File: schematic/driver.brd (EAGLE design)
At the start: 160 x 100 mm, 118 parts, among them IC1 DW01A, IC2 DW01A, IC3 DW01A, IC4 MPU6050, Q2 SI1922EDH-T1-GE3, Q3 SI1922EDH-T1-GE3, Q4 SI1922EDH-T1-GE3

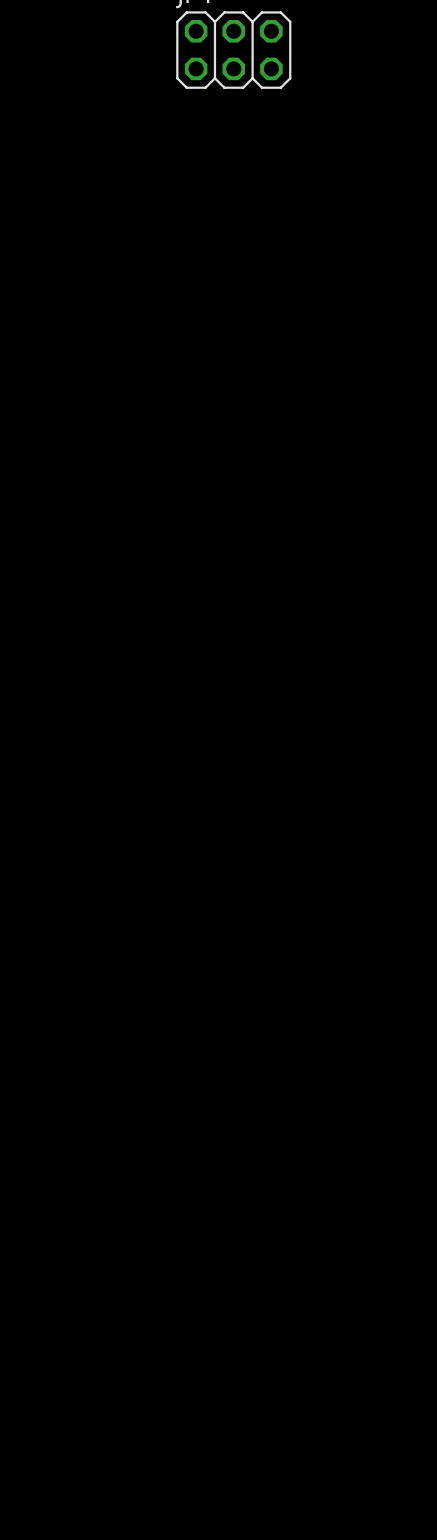
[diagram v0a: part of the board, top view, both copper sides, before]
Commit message: Added piheads for sensors. Added transoptors.
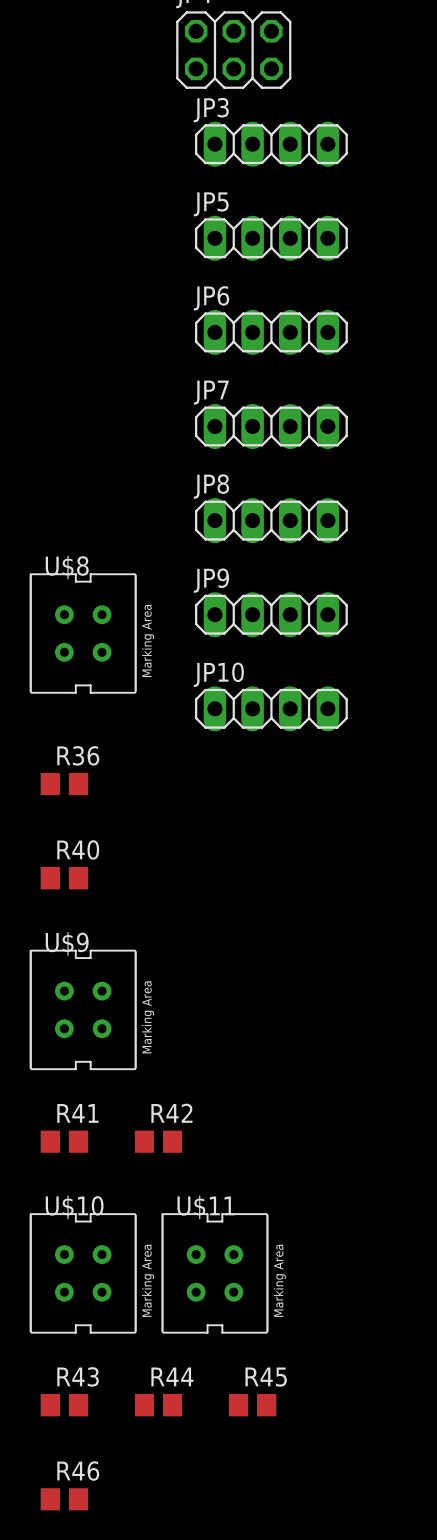
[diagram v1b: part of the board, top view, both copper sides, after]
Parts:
- added JP10, JP3, JP5, JP6, JP7, JP8, JP9: (no value), pinhead:1X04
- added R36, R41, R43, R45: 20k, rcl:R0805
- added R40, R42, R44, R46: 200, rcl:R0805
- added U$10, U$11, U$8, U$9: CNY70, cny70:4
- R35: value 50 -> 50k
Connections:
- removed net LED2: STM32.12
- removed net N$17: STM32.29
- removed net PB9: 3.3V1.A, S2.3
- removed net PC13: STM32.2
- removed net PC14: 3.3V2.A, S2.2, STM32.3
- removed net S0: STM32.18
- removed net TRST: STM32.40
- new net ADC1: R36.1, STM32.11, U$8.C
- new net ADC2: R41.1, STM32.12, U$9.C
- new net ADC3: R43.1, STM32.13, U$10.C
- new net ADC4: R45.1, U$11.C
- new net N$1: R40.1, U$8.A
- new net N$56: R42.1, U$9.A
- new net N$57: STM32.41
- new net N$62: R44.1, U$10.A
- new net N$65: R43.2, R44.2
- new net N$66: R46.1, U$11.A
- new net N$68: R45.2, R46.2
- new net SW1: 3.3V3.A, S2.1, STM32.29
- new net SW2: 3.3V2.A, S2.2, STM32.30
- new net SW3: 3.3V1.A, S2.3, STM32.31
- net BAT: now also STM32.10; no longer STM32.13
- net BUT: now also STM32.18, STM32.3; no longer STM32.19
- net GND: now also JP10.2, JP3.2, JP5.2, JP6.2, JP7.2, JP8.2, JP9.2, U$10.E, U$10.K, U$11.E, U$11.K, U$8.E, U$8.K, U$9.E, U$9.K
- net INT: now also STM32.19; no longer STM32.39
- net LED1: now also STM32.2, STM32.39, STM32.40; no longer STM32.11
- net PC15: no longer 3.3V3.A, S2.1
- net SCL2: now also JP10.3, JP3.3, JP5.3, JP6.3, JP7.3, JP8.3, JP9.3
- net SDA2: now also JP10.4, JP3.4, JP5.4, JP6.4, JP7.4, JP8.4, JP9.4
- net VCC: now also JP10.1, JP3.1, JP5.1, JP6.1, JP7.1, JP8.1, JP9.1, R36.2, R40.2, R41.2, R42.2

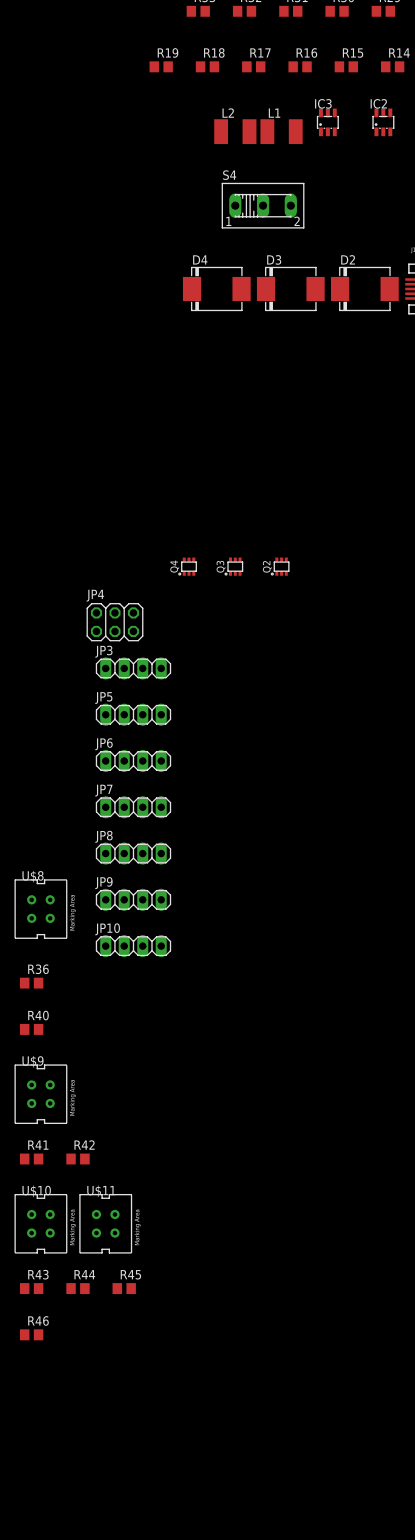
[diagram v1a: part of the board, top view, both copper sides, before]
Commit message: Pull up resistors to two I2C buses
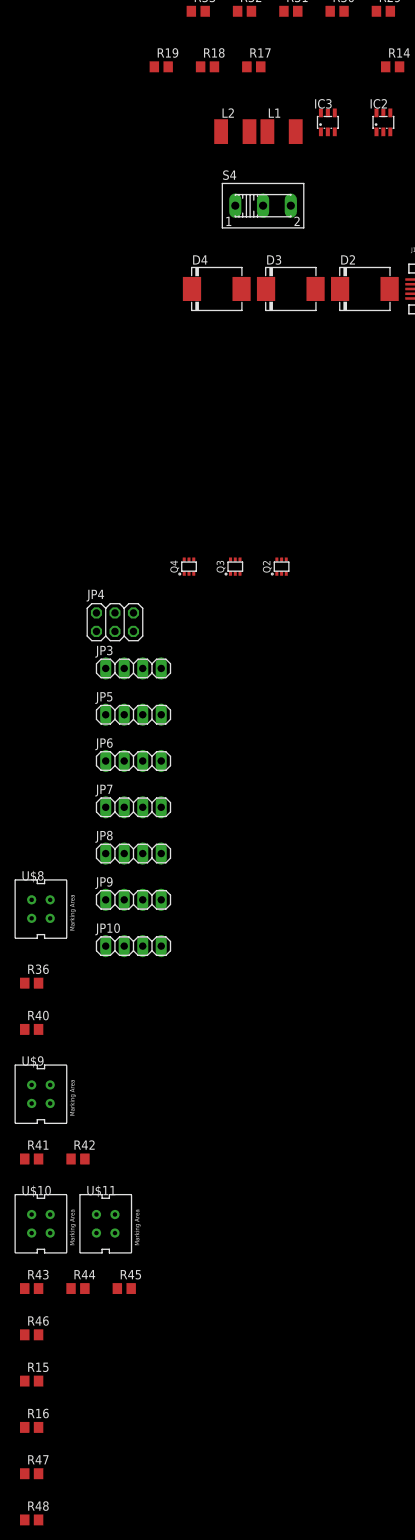
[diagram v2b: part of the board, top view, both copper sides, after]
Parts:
- added R47: 4.7k, rcl:R0805
- added R48: 4.7, rcl:R0805
- R15: value 4k7 -> 4.7k
- R16: value 4k7 -> 4.7
- moved R16 190.3 mm to (-121.9, -110.5)
- moved R15 185.4 mm to (-121.9, -104.1)
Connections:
- net SCL: no longer IC4.23, R16.1
- net SCL1: now also IC4.23, R47.1
- net SCL2: now also R15.1
- net SDA: no longer IC4.24, R15.1
- net SDA1: now also IC4.24, R48.1
- net SDA2: now also R16.1
- net VCC: no longer R15.2, R16.2
- net VDD: now also R15.2, R16.2, R47.2, R48.2
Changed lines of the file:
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@@
 <attribute name="VALUE" x="-73.025" y="73.66" size="1.27" layer="27"/>
-</element>
-<element name="R15" library="rcl" library_urn="urn:adsk.eagle:library:334" package="R0805" package3d_urn="urn:adsk.eagle:package:23553/2" value="4k7" x="-78.74" y="76.2" smashed="yes">
-<attribute name="NAME" x="-79.375" y="77.47" size="1.27" layer="25"/>
-<attribute name="POPULARITY" value="86" x="0" y="0" size="1.778" layer="27" display="off"/>
-<attribute name="SPICEPREFIX" value="R" x="0" y="0" size="1.778" layer="27" display="off"/>
-<attribute name="VALUE" x="-79.375" y="73.66" size="1.27" layer="27"/>
-</element>
-<element name="R16" library="rcl" library_urn="urn:adsk.eagle:library:334" package="R0805" package3d_urn="urn:adsk.eagle:package:23553/2" value="4k7" x="-85.09" y="76.2" smashed="yes">
-<attribute name="NAME" x="-85.725" y="77.47" size="1.27" layer="25"/>
-<attribute name="POPULARITY" value="86" x="0" y="0" size="1.778" layer="27" display="off"/>
-<attribute name="SPICEPREFIX" value="R" x="0" y="0" size="1.778" layer="27" display="off"/>
-<attribute name="VALUE" x="-85.725" y="73.66" size="1.27" layer="27"/>
 </element>
 <element name="R17" library="rcl" library_urn="urn:adsk.eagle:library:334" package="R0805" package3d_urn="urn:adsk.eagle:package:23553/2" value="10k" x="-91.44" y="76.2" smashed="yes">
@@
 <attribute name="SPICEPREFIX" value="R" x="-139.7" y="-99.06" size="1.778" layer="27" display="off"/>
 <attribute name="VALUE" x="-122.555" y="-100.33" size="1.27" layer="27"/>
+</element>
+<element name="R15" library="rcl" library_urn="urn:adsk.eagle:library:334" package="R0805" package3d_urn="urn:adsk.eagle:package:23553/2" value="4.7k" x="-121.92" y="-104.14" smashed="yes">
+<attribute name="NAME" x="-122.555" y="-102.87" size="1.27" layer="25"/>
+<attribute name="POPULARITY" value="86" x="-121.92" y="-104.14" size="1.778" layer="27" display="off"/>
+<attribute name="SPICEPREFIX" value="R" x="-121.92" y="-104.14" size="1.778" layer="27" display="off"/>
+<attribute name="VALUE" x="-122.555" y="-106.68" size="1.27" layer="27"/>
+</element>
+<element name="R16" library="rcl" library_urn="urn:adsk.eagle:library:334" package="R0805" package3d_urn="urn:adsk.eagle:package:23553/2" value="4.7" x="-121.92" y="-110.49" smashed="yes">
+<attribute name="NAME" x="-122.555" y="-109.22" size="1.27" layer="25"/>
+<attribute name="POPULARITY" value="86" x="-121.92" y="-110.49" size="1.778" layer="27" display="off"/>
+<attribute name="SPICEPREFIX" value="R" x="-121.92" y="-110.49" size="1.778" layer="27" display="off"/>
+<attribute name="VALUE" x="-122.555" y="-113.03" size="1.27" layer="27"/>
+</element>
+<element name="R47" library="rcl" library_urn="urn:adsk.eagle:library:334" package="R0805" package3d_urn="urn:adsk.eagle:package:23553/2" value="4.7k" x="-121.92" y="-116.84" smashed="yes">
+<attribute name="NAME" x="-122.555" y="-115.57" size="1.27" layer="25"/>
+<attribute name="POPULARITY" value="86" x="-121.92" y="-116.84" size="1.778" layer="27" display="off"/>
+<attribute name="SPICEPREFIX" value="R" x="-121.92" y="-116.84" size="1.778" layer="27" display="off"/>
+<attribute name="VALUE" x="-122.555" y="-119.38" size="1.27" layer="27"/>
+</element>
+<element name="R48" library="rcl" library_urn="urn:adsk.eagle:library:334" package="R0805" package3d_urn="urn:adsk.eagle:package:23553/2" value="4.7" x="-121.92" y="-123.19" smashed="yes">
+<attribute name="NAME" x="-122.555" y="-121.92" size="1.27" layer="25"/>
+<attribute name="POPULARITY" value="86" x="-121.92" y="-123.19" size="1.778" layer="27" display="off"/>
+<attribute name="SPICEPREFIX" value="R" x="-121.92" y="-123.19" size="1.778" layer="27" display="off"/>
+<attribute name="VALUE" x="-122.555" y="-125.73" size="1.27" layer="27"/>
 </element>
 </elements>
@@
 <contactref element="C4" pad="1"/>
 <contactref element="C5" pad="1"/>
-<wire x1="-113.03" y1="-1.27" x2="-113.03" y2="1.27" width="0" layer="19" extent="1-1"/>
+<contactref element="R15" pad="2"/>
+<contactref element="R16" pad="2"/>
+<contactref element="R47" pad="2"/>
+<contactref element="R48" pad="2"/>
+<wire x1="-120.97" y1="-116.84" x2="-120.97" y2="-123.19" width="0" layer="19" extent="1-1"/>
+<wire x1="-120.97" y1="-110.49" x2="-120.97" y2="-116.84" width="0" layer="19" extent="1-1"/>
+<wire x1="-120.97" y1="-104.14" x2="-120.97" y2="-110.49" width="0" layer="19" extent="1-1"/>
+<wire x1="-113.03" y1="-1.27" x2="-120.97" y2="-104.14" width="0" layer="19" extent="1-1"/>
+<wire x1="-113.03" y1="1.27" x2="-113.03" y2="-1.27" width="0" layer="19" extent="1-1"/>
 <wire x1="-61.67" y1="47.97" x2="-113.03" y2="1.27" width="0" layer="19" extent="1-1"/>
 <wire x1="-55.17" y1="47.97" x2="-61.67" y2="47.97" width="0" layer="19" extent="1-1"/>
@@
 <signal name="SCL">
 <contactref element="I2C_CON" pad="2"/>
-<contactref element="R16" pad="1"/>
-<contactref element="IC4" pad="23"/>
-<wire x1="-44.45" y1="95.25" x2="-32.45" y2="95.77" width="0" layer="19" extent="1-1"/>
-<wire x1="-86.04" y1="76.2" x2="-44.45" y2="95.25" width="0" layer="19" extent="1-1"/>
 </signal>
 <signal name="SDA">
 <contactref element="I2C_CON" pad="1"/>
-<contactref element="R15" pad="1"/>
-<contactref element="IC4" pad="24"/>
-<wire x1="-46.99" y1="95.25" x2="-32.45" y2="95.27" width="0" layer="19" extent="1-1"/>
-<wire x1="-79.69" y1="76.2" x2="-46.99" y2="95.25" width="0" layer="19" extent="1-1"/>
 </signal>
 <signal name="LED1">
@@
 </signal>
 <signal name="VCC">
-<contactref element="R16" pad="2"/>
-<contactref element="R15" pad="2"/>
 <contactref element="S2" pad="5"/>
 <contactref element="LCD1" pad="6"/>
@@
 <wire x1="-111.76" y1="-12.7" x2="-111.76" y2="-19.05" width="0" layer="19" extent="1-1"/>
 <wire x1="-111.76" y1="-6.35" x2="-111.76" y2="-12.7" width="0" layer="19" extent="1-1"/>
-<wire x1="-84.14" y1="76.2" x2="-111.76" y2="-6.35" width="0" layer="19" extent="1-1"/>
-<wire x1="-77.79" y1="76.2" x2="-84.14" y2="76.2" width="0" layer="19" extent="1-1"/>
-<wire x1="-67.31" y1="95.25" x2="-77.79" y2="76.2" width="0" layer="19" extent="1-1"/>
+<wire x1="-34.02" y1="36.05" x2="-111.76" y2="-6.35" width="0" layer="19" extent="1-1"/>
+<wire x1="-33.02" y1="49.53" x2="-34.02" y2="36.05" width="0" layer="19" extent="1-1"/>
+<wire x1="-23.27" y1="76.2" x2="-33.02" y2="49.53" width="0" layer="19" extent="1-1"/>
+<wire x1="-46.04" y1="76.2" x2="-23.27" y2="76.2" width="0" layer="19" extent="1-1"/>
+<wire x1="-52.39" y1="90.17" x2="-46.04" y2="76.2" width="0" layer="19" extent="1-1"/>
+<wire x1="-67.31" y1="95.25" x2="-52.39" y2="90.17" width="0" layer="19" extent="1-1"/>
 <wire x1="-69.43" y1="107.95" x2="-67.31" y2="95.25" width="0" layer="19" extent="1-1"/>
 <wire x1="-75.78" y1="107.95" x2="-69.43" y2="107.95" width="0" layer="19" extent="1-1"/>
 <wire x1="-82.13" y1="102.87" x2="-75.78" y2="107.95" width="0" layer="19" extent="1-1"/>
-<wire x1="-52.39" y1="90.17" x2="-67.31" y2="95.25" width="0" layer="19" extent="1-1"/>
-<wire x1="-46.04" y1="76.2" x2="-52.39" y2="90.17" width="0" layer="19" extent="1-1"/>
-<wire x1="-23.27" y1="76.2" x2="-46.04" y2="76.2" width="0" layer="19" extent="1-1"/>
-<wire x1="-33.02" y1="49.53" x2="-23.27" y2="76.2" width="0" layer="19" extent="1-1"/>
-<wire x1="-34.02" y1="36.05" x2="-33.02" y2="49.53" width="0" layer="19" extent="1-1"/>
 <wire x1="48.17" y1="72.0875" x2="-23.27" y2="76.2" width="0" layer="19" extent="1-16"/>
 <wire x1="48.17" y1="71.4375" x2="48.17" y2="72.0875" width="0" layer="19" extent="16-16"/>
@@
 <signal name="SCL1">
 <contactref element="STM32" pad="42"/>
+<contactref element="IC4" pad="23"/>
+<contactref element="R47" pad="1"/>
+<wire x1="-32.45" y1="95.77" x2="-122.87" y2="-116.84" width="0" layer="19" extent="1-1"/>
+<wire x1="37.648759375" y1="50.33479375" x2="-32.45" y2="95.77" width="0" layer="19" extent="1-16"/>
 </signal>
 <signal name="SDA1">
 <contactref element="STM32" pad="43"/>
+<contactref element="IC4" pad="24"/>
+<contactref element="R48" pad="1"/>
+<wire x1="37.29520625" y1="49.981240625" x2="-122.87" y2="-123.19" width="0" layer="19" extent="1-16"/>
+<wire x1="-32.45" y1="95.27" x2="37.29520625" y2="49.981240625" width="0" layer="19" extent="1-16"/>
 </signal>
 <signal name="BOOT0">
@@
 <contactref element="JP6" pad="4"/>
 <contactref element="JP5" pad="4"/>
+<contactref element="R16" pad="1"/>
+<wire x1="-104.14" y1="-44.45" x2="-122.87" y2="-110.49" width="0" layer="19" extent="1-1"/>
 <wire x1="-104.14" y1="-38.1" x2="-104.14" y2="-44.45" width="0" layer="19" extent="1-1"/>
 <wire x1="-104.14" y1="-31.75" x2="-104.14" y2="-38.1" width="0" layer="19" extent="1-1"/>
@@
 <contactref element="JP6" pad="3"/>
 <contactref element="JP5" pad="3"/>
+<contactref element="R15" pad="1"/>
+<wire x1="-106.68" y1="-44.45" x2="-122.87" y2="-104.14" width="0" layer="19" extent="1-1"/>
 <wire x1="-106.68" y1="-38.1" x2="-106.68" y2="-44.45" width="0" layer="19" extent="1-1"/>
 <wire x1="-106.68" y1="-31.75" x2="-106.68" y2="-38.1" width="0" layer="19" extent="1-1"/>

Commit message: ułożenie pinów i podpięcie sterowników rage quit
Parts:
- removed 3.3V1, 3.3V2, 3.3V3: (no value), led:CHIPLED_0805
- removed C1, C15, C2, C4, C5: 100n, rcl:C0603
- removed C10, C11: (no value), rcl:C0603
- removed C16: 4,7u, rcl:C0603
- removed I2C_CON, JP10, JP3, JP5, JP6, JP7, JP8, JP9: (no value), pinhead:1X04
- removed Q1: (no value), crystal-geyer_V1_0:3.2X2.5_KX-7
- removed R5, R6, R9: 1k, rcl:R0805
- added BATTERY: (no value), pinhead:1X02
- added CELLS: (no value), Connectors:HDR-04/RA
- added DIS1, DIS2, DIS3, DIS4, DIS5, DIS6, DIS7, JP13, JP14: (no value), pinhead:1X04
- added JP11, JP12: (no value), pinhead:1X03
- added XTAL: (no value), crystal-geyer_V1_0:3.2X2.5_KX-7
- added _C1, _C2: (no value), rcl:C0603
- added _C3, _C4, _C5, _C7: 100n, rcl:C0603
- added _C6: 4,7u, rcl:C0603
- added _C8: 10n, rcl:C0603
- added _C9: 1uF, rcl:C0603
- D2, D3, D4, D5, D6, D7: value S3A -> (none); device s3x_10:DO214AB -> adafruit:CHIPLED-0603-TTW
- JP2: device pinhead:1X02 -> pinhead:2X14
- Q2: value SI1922EDH-T1-GE3 -> MOSFET1
- Q3: value SI1922EDH-T1-GE3 -> MOSFET2
- Q4: value SI1922EDH-T1-GE3 -> MOSFET3
- STM32: value STM32F10XCXT6 -> (none)
- moved U$10 238.2 mm to (86.0, 36.0), flipped to the bottom
- moved L2 230.7 mm to (105.5, -48.5), turned to 90 degrees
- moved L1 219.1 mm to (104.7, -37.7), turned to 90 degrees
- moved R48 215.3 mm to (-105.4, 91.4)
- moved IC3 205.0 mm to (90.0, -44.0)
- moved Q4 201.1 mm to (94.0, -44.0)
- moved R47 201.0 mm to (-66.0, 76.2)
- moved IC1 196.6 mm to (90.0, -51.0)
- moved IC2 194.8 mm to (90.0, -37.0)
- moved JP4 193.8 mm to (81.7, 24.9), turned to 90 degrees
- moved Q3 193.2 mm to (94.0, -37.0)
- moved U$5 191.1 mm to (99.0, -39.0), turned to 90 degrees
- moved Q2 190.9 mm to (94.0, -51.0)
- moved R15 190.8 mm to (-59.7, 76.2)
- moved R46 190.6 mm to (-99.1, 91.4)
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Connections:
- removed net AO1: MB.1, U$7.5, U$7.6, U$7.7, U$7.8
- removed net N$48: C27.1, C28.1, U$6.24
- removed net N$52: 3.3V2.C, R6.2
- removed net N$53: 3.3V3.C, R5.2
- removed net N$57: STM32.41
- removed net SCL: I2C_CON.2
- removed net SDA: I2C_CON.1
- removed net VSS: STM32.8
- new net ...: STM32.25
- new net ADC5: JP11.3, STM32.39
- new net ADC6: JP12.3, STM32.40
- new net N$17: JP14.3
- new net N$64: MB.2, U$7.5, U$7.6, U$7.7, U$7.8
- net A01: now also MA.1; no longer MA.2
- net A02: now also MB.1; no longer MB.2
- net ADC4: now also STM32.19
- net AO2: now also MA.2; no longer MA.1
- net BAT+: now also BATTERY.2; no longer JP2.2
- net BAT_ON: now also C27.1, C28.1, U$6.24
- net BUT: no longer STM32.18
- net CELL1: now also CELLS.2
- net CELL2: now also CELLS.3
- net CELL3: now also CELLS.4
- net GND: now also BATTERY.1, CELLS.1, DIS1.2, DIS2.2, DIS3.2, DIS4.2, DIS5.2, DIS6.2, DIS7.2, JP11.2, JP12.2, JP13.3, S2.1, S2.2, S2.3, STM32.8, _C1.2, _C2.2, _C3.2, _C4.2, _C5.2, _C6.2, _C7.2, _C8.2, _C9.2; no longer C1.2, C10.2, C11.2, C15.2, C16.2, C2.2, C4.2, C5.2, I2C_CON.3, JP10.2, JP2.1, JP3.2, JP5.2, JP6.2, JP7.2, JP8.2, JP9.2, R5.1, R6.1, R9.1
- net INT: now also STM32.18; no longer STM32.19
- net LED1: no longer STM32.39, STM32.40
- net MA1: now also STM32.41; no longer STM32.25
- net MA2: now also STM32.45; no longer STM32.46
- net N$12: now also D2.C@1; no longer D2.C
- net N$14: now also D3.C@1; no longer D3.C
- net N$18: now also D4.C@1; no longer D4.C
- net N$19: now also D5.C@1; no longer D5.C
- net N$2: now also JP14.4; no longer 3.3V1.C, R9.2
- net N$24: now also D6.C@1; no longer D6.C
- net N$25: now also D7.C@1; no longer D7.C
- net N$3: now also XTAL.1, _C2.1; no longer C11.1, Q1.1
- net N$4: now also XTAL.3, _C1.1; no longer C10.1, Q1.3
- net PWMA: now also STM32.46; no longer STM32.45
- net SCL2: now also DIS1.3, DIS2.3, DIS3.3, DIS4.3, DIS5.3, DIS6.3, DIS7.3, JP13.2; no longer JP10.3, JP3.3, JP5.3, JP6.3, JP7.3, JP8.3, JP9.3
- net SDA2: now also DIS1.4, DIS2.4, DIS3.4, DIS4.4, DIS5.4, DIS6.4, DIS7.4, JP13.1; no longer JP10.4, JP3.4, JP5.4, JP6.4, JP7.4, JP8.4, JP9.4
- net SW1: no longer 3.3V3.A, S2.1
- net SW2: no longer 3.3V2.A, S2.2
- net SW3: no longer 3.3V1.A, S2.3
- net SWDA: now also STM32.34
- net SWDIO: no longer STM32.34
- net VCC: now also DIS1.1, DIS2.1, DIS3.1, DIS4.1, DIS5.1, DIS6.1, DIS7.1, JP11.1, JP12.1, JP13.4; no longer JP10.1, JP3.1, JP5.1, JP6.1, JP7.1, JP8.1, JP9.1
- net VCC_S: no longer I2C_CON.4
- net VDD: now also _C3.1, _C4.1, _C5.1, _C6.1, _C7.1, _C8.1, _C9.1; no longer C1.1, C15.1, C16.1, C2.1, C4.1, C5.1
- net VUSB: now also D2.A@1, D3.A@1, D4.A@1, D5.A@1, D6.A@1, D7.A@1; no longer D2.A, D3.A, D4.A, D5.A, D6.A, D7.A
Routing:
- net GND: track 0.00 -> 98.7 mm, vias 0 -> 2
- net BOOT0: track 0.00 -> 39.8 mm
- net PWMA: track 0.00 -> 31.6 mm, vias 0 -> 2
- net VDD: track 0.00 -> 24.6 mm
- net MA2: track 0.00 -> 22.0 mm
- net MA1: track 0.00 -> 20.1 mm, vias 0 -> 2
- net BAT_ON: track 0.00 -> 17.3 mm, vias 0 -> 2
- net AO2: track 0.00 -> 13.3 mm
- net N$53: track 0.00 -> 12.8 mm
- net N$4: track 0.00 -> 11.7 mm
- net N$60: track 0.00 -> 10.7 mm
- net BUT: track 0.00 -> 8.44 mm
- net N$3: track 0.00 -> 8.17 mm
- net A01: track 0.00 -> 7.94 mm
- net N$67: track 0.00 -> 7.90 mm
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- added copper zone on layer 16, net VCC
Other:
- board size 160 x 100 mm -> 90 x 40 mm

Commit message: s
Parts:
- moved U$8 118.0 mm to (45.0, -35.5)
- moved JP2 43.5 mm to (-22.0, -14.0)
- moved MB 43.4 mm to (48.0, -21.0)
- moved MA 33.6 mm to (42.0, -21.0)
- moved BATTERY 26.0 mm to (27.0, 4.01)
- moved STM32 14.1 mm to (31.0, 23.0)
- moved _C5 14.1 mm to (29.0, 14.0)
- moved _C8 14.1 mm to (22.0, 20.0)
- moved U$6 14.1 mm to (48.0, 15.0)
- moved XTAL 14.1 mm to (23.6, 15.3)
- moved _C3 14.1 mm to (28.0, 31.0)
- moved _C4 14.1 mm to (39.0, 26.0)
- moved _C6 14.1 mm to (34.0, 14.0)
- moved _C7 14.1 mm to (31.6, 13.9)
- moved _C1 14.1 mm to (22.0, 12.0)
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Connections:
- net A02 renamed B01
- net N$64 renamed B02
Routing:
- net B01: track 0.00 -> 30.3 mm
- net GND: track 98.7 -> 68.8 mm, vias 2 -> 0
- net B02: track 0.00 -> 27.7 mm
- net AO2: track 13.3 -> 30.2 mm
- net A01: track 7.94 -> 24.2 mm
- net BAT_ON: track 17.3 -> 1.80 mm, vias 2 -> 1
- net BOOT0: track 39.8 -> 53.0 mm
- net N$53: track 12.8 -> 0.00 mm
- net N$67: track 7.90 -> 0.00 mm
- net N$69: track 7.83 -> 0.00 mm
- net N$59: track 6.32 -> 0.00 mm
- net N$52: track 6.20 -> 0.00 mm
- net N$48: track 6.83 -> 10.7 mm
- net N$46: track 3.22 -> 6.20 mm
- net N$57: track 2.68 -> 0.00 mm
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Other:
- board size 90 x 40 mm -> 90 x 79.5 mm
